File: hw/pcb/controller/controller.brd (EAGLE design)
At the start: 160 x 100 mm, 0 parts

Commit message: Draft of schematic is complete
Still needs review.
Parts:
- added C1, C10, C11, C12, C13, C14, C15, C16, C17, C18, C2, C3, C4, C5, C6, C7, C8, C9: (no value), wedfestdress:CAP_0603
- added D1, D2: (no value), wedfestdress:LED_0603
- added D3: (no value), wedfestdress:LED_0603_OSRAM
- added FB1: (no value), wedfestdress:FB_0603
- added J1: (no value), wedfestdress:10118192-0001LF
- added J10: (no value), wedfestdress:MOLEX_MICROLOCK_RA_2_POS
- added J11: (no value), wedfestdress:MOLEX_MICROLOCK_RA_3_POS
- added J12: (no value), wedfestdress:DF13-3P-1.25H
- added J2: (no value), wedfestdress:MOLEX_MICROFIT_2POS_SMT_RA_W_BOSSES
- added J3: (no value), wedfestdress:DF13-5P-1.25H
- added J4, J5, J6, J7, J8, J9: (no value), wedfestdress:MOLEX_MICROLOCK_RA_4_POS
- added R1, R10, R11, R12, R13, R14, R15, R16, R17, R18, R19, R2, R20, R21, R22, R23, R24, R25, R26, R27, R28, R29, R3, R30, R31, R4, R5, R6, R7, R8, R9: (no value), wedfestdress:RES_0603
- added SW1, SW2, SW3: KMR221NG, wedfestdress:KMR2
- added SW4: CL-SB-22B-12T, wedfestdress:CL-SB-22B-12T
- added TP1, TP10, TP11, TP2, TP3, TP4, TP5, TP6, TP7, TP8, TP9: (no value), wedfestdress:TP_1P6_MM_ROUND
- added TVS1, TVS10, TVS11, TVS12, TVS13, TVS14, TVS15, TVS16, TVS17, TVS18, TVS19, TVS2, TVS20, TVS21, TVS22, TVS23, TVS24, TVS25, TVS26, TVS27, TVS3, TVS4, TVS5, TVS6, TVS7, TVS8, TVS9: (no value), wedfestdress:SOD523
- added U1: (no value), wedfestdress:LQFP64_0P5MM_10X10MM
- added U10, U11, U12, U13, U14, U15, U4, U5, U6, U7, U8, U9: (no value), wedfestdress:SC-70-6_GENERIC
- added U16, U17, U18, U19, U20, U3: (no value), wedfestdress:SOT-23-6_GENERIC
- added U2: (no value), wedfestdress:TOSHIBA_SMV
- added U21: (no value), wedfestdress:SC-70-5_GENERIC
- added U22: (no value), wedfestdress:SOT65P210X110-6N
- added U23: (no value), wedfestdress:ADXL337
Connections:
- new net +6V: C9.P$1, J1.P$1, R1.P$2, TVS26.K
- new net 3V3: C11.P$1, C12.P$1, C13.P$2, C15.P$1, C2.P$1, C3.P$1, C4.P$1, C5.P$1, C6.P$1, C7.P$1, C8.P$1, FB1.P$1, J11.P2, J3.P$1, R17.P$2, R19.P$2, R22.P$2, R23.P$2, R26.P$2, R5.P$2, R6.P$2, R7.P$1, R8.P$2, TP11.P$1, TP5.P$1, TP7.P$1, TVS4.K, U1.24, U1.34, U1.56, U1.8, U10.5, U11.5, U12.5, U13.5, U14.5, U15.5, U2.P5, U21.5, U22.1, U23.P14, U23.P15, U4.5, U5.5, U6.5, U7.5, U8.5, U9.5
- new net ACCEL_TEST: TP1.P$1, U23.P2
- new net ACCEL_XOUT: C18.P$1, U1.14, U23.P5
- new net ACCEL_YOUT: C17.P$1, U1.15, U23.P4
- new net ACCEL_ZOUT: C16.P$1, U1.16, U23.P16
- new net AUX_BTN: R26.P$1, SW3.P1, U1.59
- new net BATT_DIV2: C14.P$1, R24.P$1, R25.P$2, U1.18
- new net CLKOUT: TP6.P$1, U1.61
- new net FC0_MOSI: U1.63, U4.3, U6.3, U8.3
- new net FC0_SCK: U1.60, U5.3, U7.3, U9.3
- new net FC1_RXD: J12.P$2, U1.11
- new net FC1_TXD: J12.P$3, U1.12
- new net FC2_MOSI: U1.43, U10.3, U12.3, U14.3
- new net FC2_SCK: U1.45, U11.3, U13.3, U15.3
- new net FC5_SCL: R23.P$1, U1.54, U22.3
- new net FC5_SDA: R22.P$1, U1.51, U22.4
- new net FC6_RXD: TP3.P$1, U1.39
- new net FC6_TXD: TP2.P$1, U1.40
- new net GND: C1.P$2, C10.P$2, C11.P$2, C12.P$2, C13.P$1, C15.P$2, C16.P$2, C17.P$2, C18.P$2, C2.P$2, C3.P$2, C4.P$2, C5.P$2, C6.P$2, C7.P$2, C8.P$2, C9.P$2, J1.P$5, J10.P1, J11.P1, J12.P$1, J2.P1, J3.P$2, J4.P1, J5.P1, J6.P1, J7.P1, J8.P1, J9.P1, R16.P$1, R18.P$1, R2.P$1, R28.P$1, R29.P$1, R30.P$1, R31.P$1, SW1.P1, SW2.P3, SW3.P3, TP10.P$1, TP4.P$1, TP8.P$1, TP9.P$1, TVS1.A, TVS10.A, TVS11.A, TVS12.A, TVS13.A, TVS14.A, TVS15.A, TVS16.A, TVS17.A, TVS18.A, TVS19.A, TVS2.A, TVS20.A, TVS21.A, TVS22.A, TVS23.A, TVS24.A, TVS25.A, TVS26.A, TVS27.A, TVS3.A, TVS4.A, TVS5.A, TVS6.A, TVS7.A, TVS8.A, TVS9.A, U1.20, U1.21, U1.25, U1.55, U1.9, U10.2, U11.2, U12.2, U13.2, U14.2, U15.2, U16.1, U17.1, U18.1, U19.1, U2.P2, U20.1, U21.2, U22.2, U23.P6, U23.P7, U3.1, U4.2, U5.2, U6.2, U7.2, U8.2, U9.2
- new net GREEN_LED1: D1.A, U1.49
- new net GREEN_LED2: D2.A, U1.50
- new net ISP0: R8.P$1, SW2.P1, U1.13
- new net ISP1: R7.P$2, U1.38
- new net LED_PWR_EN: R16.P$2, U1.36, U20.5, U3.5
- new net MIC_AMP_OUT: R21.P$2, U1.17, U21.4, U22.6
- new net MIC_IN: J11.P3, R20.P$1
- new net N$1: R10.P$2, U3.6
- new net N$10: D3.K, R29.P$2
- new net N$11: D2.K, R30.P$2
- new net N$12: D1.K, R31.P$2
- new net N$16: R15.P$2, U20.6
- new net N$17: R11.P$2, U16.6
- new net N$19: R12.P$2, U17.6
- new net N$2: R3.P$2, U1.5
- new net N$21: R13.P$2, U18.6
- new net N$23: R14.P$2, U19.6
- new net N$3: R4.P$2, U1.6
- new net N$4: J1.P$2, R4.P$1, TVS2.K
- new net N$5: J1.P$3, R3.P$1, R5.P$1, TVS1.K
- new net N$6: R9.P$1, U2.P3
- new net N$7: R20.P$2, R21.P$1, U21.3, U22.5
- new net N$9: C14.P$2, R25.P$1, R27.P$1, R28.P$2
- new net RED_LED1: D3.A, U1.58
- new net RESET_N: J3.P$3, R6.P$1, SW1.P3, TVS5.K, U1.64
- new net STRING1_CLK: J4.P2, TVS23.K, U5.4
- new net STRING1_DATA: J4.P4, TVS25.K, U4.4
- new net STRING1_EN: U1.1, U4.1, U5.1
- new net STRING1_V+: J4.P3, TVS24.K, U3.2, U3.3, U4.6, U5.6
- new net STRING2_CLK: J5.P2, TVS20.K, U7.4
- new net STRING2_DATA: J5.P4, TVS22.K, U6.4
- new net STRING2_EN: U1.2, U6.1, U7.1
- new net STRING2_V+: J5.P3, TVS21.K, U16.2, U16.3, U6.6, U7.6
- new net STRING3_CLK: J6.P2, TVS17.K, U9.4
- new net STRING3_DATA: J6.P4, TVS19.K, U8.4
- new net STRING3_EN: U1.3, U8.1, U9.1
- new net STRING3_V+: J6.P3, TVS18.K, U17.2, U17.3, U8.6, U9.6
- new net STRING4_CLK: J7.P2, TVS14.K, U11.4
- new net STRING4_DATA: J7.P4, TVS16.K, U10.4
- new net STRING4_EN: U1.46, U10.1, U11.1
- new net STRING4_V+: J7.P3, TVS15.K, U10.6, U11.6, U18.2, U18.3
- new net STRING5_CLK: J8.P2, TVS11.K, U13.4
- new net STRING5_DATA: J8.P4, TVS13.K, U12.4
- new net STRING5_EN: U1.47, U12.1, U13.1
- new net STRING5_V+: J8.P3, TVS12.K, U12.6, U13.6, U19.2, U19.3
- new net STRING6_CLK: J9.P2, TVS8.K, U15.4
- new net STRING6_DATA: J9.P4, TVS10.K, U14.4
- new net STRING6_EN: U1.48, U14.1, U15.1
- new net STRING6_V+: J9.P3, TVS9.K, U14.6, U15.6, U20.2, U20.3
- new net SWCLK: J3.P$4, TVS6.K, U1.52
- new net SWDIO: J3.P$5, TVS7.K, U1.53
- new net USB_VBUS: R1.P$1, R2.P$2, U1.26
- new net USER_BTN_IN: J10.P2, R17.P$1, U1.10
- new net VBAT: J2.P2, R10.P$1, R11.P$1, R12.P$1, R13.P$1, R14.P$1, R15.P$1, R24.P$2, SW4.3, SW4.4, TVS27.K, U16.4, U17.4, U18.4, U19.4, U20.4, U3.4
- new net VBAT_READ_EN_R: R27.P$2, U1.42
- new net VBAT_SW: C10.P$1, R9.P$2, SW4.5, SW4.6, TVS3.K, U2.P1
- new net VDDA: C1.P$1, FB1.P$2, U1.22, U1.23
- new net VREF: R18.P$2, R19.P$1, U21.1

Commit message: Routing and silscreen cleanup complete
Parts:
- removed R27, R28: (no value), wedfestdress:RES_0603
- added TP12: (no value), wedfestdress:TP_1P6_MM_ROUND
- added TVS28, TVS29, TVS30: (no value), wedfestdress:SOD523
- moved R31 530.5 mm to (16.8, 38.0)
- moved R30 523.9 mm to (16.8, 35.2)
- moved R29 517.4 mm to (16.8, 32.4)
- moved TP8 517.2 mm to (7.70, 52.3)
- moved D2 514.3 mm to (20.3, 35.2), turned to 180 degrees
- moved TP7 513.2 mm to (29.8, 48.0)
- moved TVS27 513.0 mm to (17.7, 17.7), flipped to the bottom, turned to 135 degrees
- moved R26 509.1 mm to (23.3, 27.1), turned to 270 degrees
- moved TP5 503.6 mm to (52.0, 41.3), turned to 270 degrees
- moved TP10 500.0 mm to (27.5, 27.4)
- moved TP4 498.8 mm to (52.0, 38.9), turned to 270 degrees
- moved TP11 496.2 mm to (36.9, 19.6)
- moved TP6 496.0 mm to (25.8, 33.8)
- moved TP3 493.9 mm to (52.0, 36.5), turned to 270 degrees
- moved TP2 489.0 mm to (52.0, 34.1), turned to 270 degrees
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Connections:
- net N$7 renamed AMP_NEG
- removed net N$9: C14.P$2, R25.P$1, R27.P$1, R28.P$2
- removed net VBAT_READ_EN_R: R27.P$2, U1.42
- net 3V3: now also TP12.P$1, TVS29.K
- net GND: now also C14.P$2, R25.P$1, TVS28.A, TVS29.A, TVS30.A; no longer R28.P$1
- net LED_PWR_EN: now also U16.5, U17.5, U18.5, U19.5
- net MIC_IN: now also TVS30.K
- net STRING1_CLK: now also J4.P3; no longer J4.P2
- net STRING1_V+: now also J4.P2; no longer J4.P3
- net STRING2_CLK: now also J5.P3; no longer J5.P2
- net STRING2_V+: now also J5.P2; no longer J5.P3
- net STRING3_CLK: now also J6.P3; no longer J6.P2
- net STRING3_V+: now also J6.P2; no longer J6.P3
- net STRING4_CLK: now also J7.P3; no longer J7.P2
- net STRING4_V+: now also J7.P2; no longer J7.P3
- net STRING5_CLK: now also J8.P3; no longer J8.P2
- net STRING5_V+: now also J8.P2; no longer J8.P3
- net STRING6_CLK: now also J9.P3; no longer J9.P2
- net STRING6_V+: now also J9.P2; no longer J9.P3
- net USER_BTN_IN: now also TVS28.K
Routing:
- net GND: track 0.00 -> 152.5 mm, vias 0 -> 62
- net 3V3: track 0.00 -> 131.6 mm, vias 0 -> 27
- net LED_PWR_EN: track 0.00 -> 114.0 mm, vias 0 -> 7
- net FC2_MOSI: track 0.00 -> 61.9 mm, vias 0 -> 6
- net FC2_SCK: track 0.00 -> 59.0 mm, vias 0 -> 2
- net STRING6_EN: track 0.00 -> 53.0 mm, vias 0 -> 2
- net N$5: track 0.00 -> 51.9 mm, vias 0 -> 2
- net RESET_N: track 0.00 -> 51.4 mm, vias 0 -> 4
- net FC0_MOSI: track 0.00 -> 50.5 mm, vias 0 -> 6
- net MIC_AMP_OUT: track 0.00 -> 50.0 mm, vias 0 -> 3
- net FC0_SCK: track 0.00 -> 48.7 mm, vias 0 -> 2
- net STRING5_EN: track 0.00 -> 46.4 mm, vias 0 -> 2
- net N$4: track 0.00 -> 46.0 mm, vias 0 -> 2
- net STRING4_EN: track 0.00 -> 43.0 mm, vias 0 -> 2
- net STRING3_EN: track 0.00 -> 35.7 mm, vias 0 -> 2
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- added copper zone on layer 15, net 3V3
- added copper zone on layer 1, net GND
- added copper zone on layer 2, net GND
- added copper zone on layer 1, net VBAT
- added copper zone on layer 15, net VBAT
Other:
- board size 160 x 100 mm -> 60 x 60 mm
- board text added: "+"
- board text added: "+X"
- board text added: "+Y"
- board text added: "+Z"
- board text added: "-"
- board text added: "BAD"
- board text added: "BTN"
- board text added: "BTN2"
- board text added: "ISP"
- board text added: "LED1"
- board text added: "LED2"
- board text added: "MIC"
- board text added: "RESET"
- board text added: "Rev A"
- board text added: "Rx"
- board text added: "S1"
- board text added: "S2"
- board text added: "S3"
- board text added: "S4"
- board text added: "S5"
- board text added: "S6"
- board text added: "Tx"
- board text added: "V+"
- board text added: "Wedfestdress!"

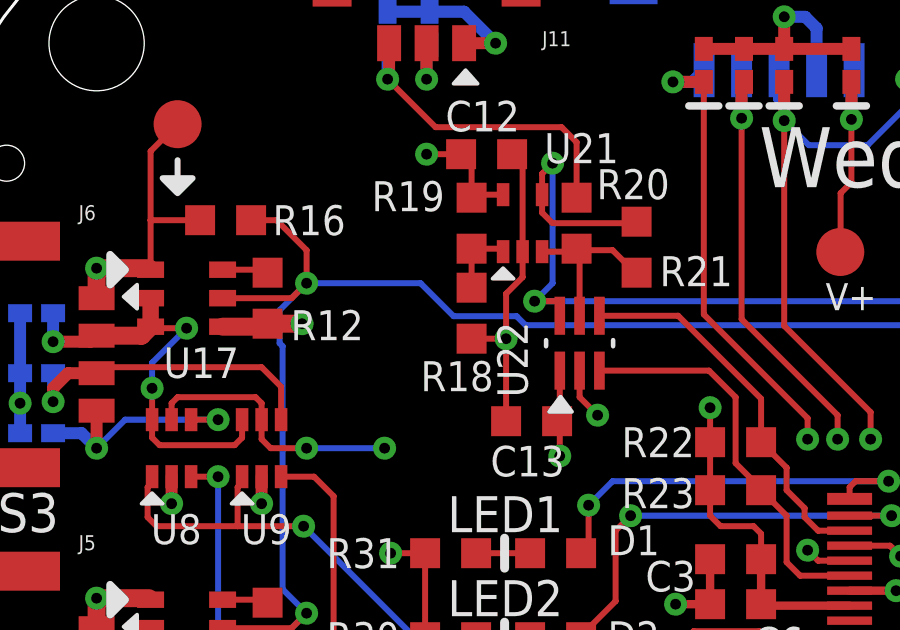
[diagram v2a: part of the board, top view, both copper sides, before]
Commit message: Add microphone board
Completed schematic and layout of microphone board. Is a similar
design to the one from TI's tidu765 app-note. Has provisions for a
more basic non-inverting amplifier design as well. Currently uses a
transimpedence amplifier.
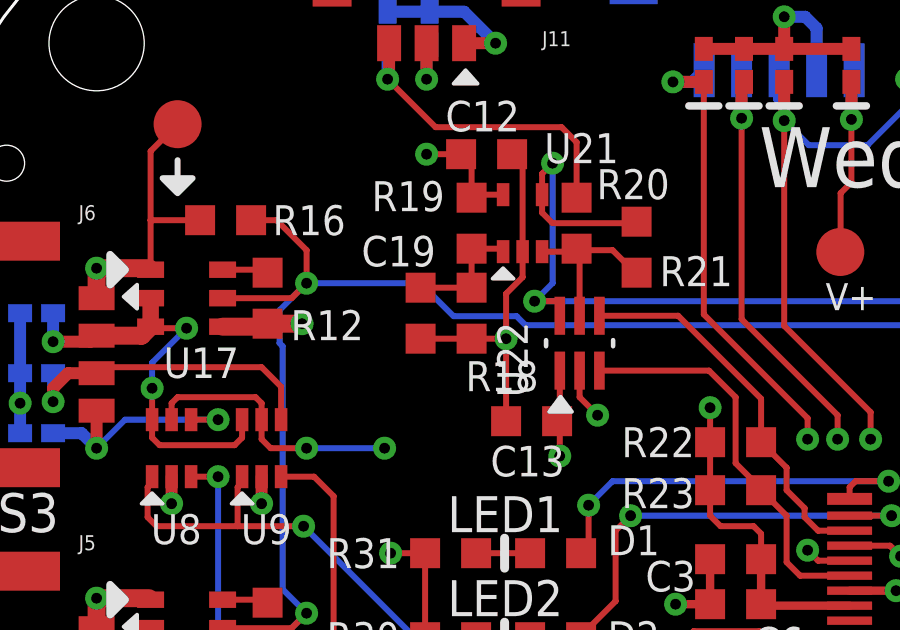
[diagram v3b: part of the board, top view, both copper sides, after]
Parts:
- added C19: (no value), wedfestdress:CAP_0603
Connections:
- net GND: now also C19.P$2
- net VREF: now also C19.P$1
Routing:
- net VREF: track 2.39 -> 4.09 mm
- net GND: track 152.5 -> 154.2 mm
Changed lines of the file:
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@@
 <layer number="21" name="tPlace" color="7" fill="1" visible="yes" active="yes"/>
 <layer number="22" name="bPlace" color="7" fill="1" visible="yes" active="yes"/>
-<layer number="23" name="tOrigins" color="15" fill="1" visible="no" active="yes"/>
+<layer number="23" name="tOrigins" color="15" fill="1" visible="yes" active="yes"/>
 <layer number="24" name="bOrigins" color="15" fill="1" visible="no" active="yes"/>
 <layer number="25" name="tNames" color="7" fill="1" visible="no" active="yes"/>
@@
 <attribute name="NOSTUFF" value="" x="17.5" y="46" size="1.778" layer="27" rot="R90" display="off"/>
 <attribute name="COST_X500" value=".00382" x="17.5" y="46" size="1.778" layer="27" rot="R90" display="off"/>
-<attribute name="NAME" x="18.23" y="44.4" size="1" layer="21" font="vector" rot="R180"/>
+<attribute name="NAME" x="19.73" y="44.4" size="1" layer="21" font="vector" rot="R180"/>
 <attribute name="NAME" x="18.5" y="47.27" size="1" layer="105" font="vector" rot="R90"/>
 </element>
@@
 <attribute name="COST_X500" value="0.22626" x="14.7" y="55.5" size="1.778" layer="28" rot="MR270" display="off"/>
 </element>
+<element name="C19" library="wedfestdress" package="CAP_0603" value="" x="15.8" y="46" smashed="yes" rot="R270">
+<attribute name="PACKAGE" value="0603" x="15.8" y="46" size="0.9" layer="27" font="vector" ratio="10" rot="R270" display="off"/>
+<attribute name="DIST_PART_NO" value="490-3894-1-ND" x="15.8" y="46" size="0.9" layer="27" font="vector" ratio="10" rot="R270" display="off"/>
+<attribute name="COST_X1" value="0.11" x="15.8" y="46" size="0.9" layer="27" font="vector" ratio="10" rot="R270" display="off"/>
+<attribute name="DISTRIBUTOR" value="Digikey" x="15.8" y="46" size="0.9" layer="27" font="vector" ratio="10" rot="R270" display="off"/>
+<attribute name="DESCRIPTION" value="Capacitor, 1 uF, 16V, 0603, X5R" x="15.8" y="46" size="0.9" layer="27" font="vector" ratio="10" rot="R270" display="off"/>
+<attribute name="DISPLAY" value="1 uF, 50V" x="15.8" y="46" size="0.9" layer="27" font="vector" ratio="10" rot="R270" display="off"/>
+<attribute name="COST_X100" value="0.0356" x="15.8" y="46" size="0.9" layer="27" font="vector" ratio="10" rot="R270" display="off"/>
+<attribute name="MFG" value="Murata" x="15.8" y="46" size="0.9" layer="27" font="vector" ratio="10" rot="R270" display="off"/>
+<attribute name="MFG_PART_NO" value="GRM185R61C105KE44D" x="15.8" y="46" size="0.9" layer="27" font="vector" ratio="10" rot="R270" display="off"/>
+<attribute name="NOSTUFF" value="" x="15.8" y="46" size="0.9" layer="27" font="vector" ratio="10" rot="R270" display="off"/>
+<attribute name="COST_X500" value="0.02512" x="15.8" y="46" size="0.9" layer="27" font="vector" ratio="10" rot="R270" display="off"/>
+<attribute name="NAME" x="13.83" y="47.56" size="1.016" layer="21" font="vector"/>
+</element>
 </elements>
 <signals>
@@
 <wire x1="27.49" y1="27.42" x2="28.8" y2="28.73" width="0.2" layer="1"/>
 <via x="28.8" y="28.73" extent="1-16" drill="0.36" diameter="0.61"/>
+<contactref element="C19" pad="P$2"/>
+<wire x1="15.8" y1="45.15" x2="17.5" y2="45.15" width="0.2" layer="1"/>
 </signal>
 <signal name="3V3">
@@
 <wire x1="17.5" y1="48.15" x2="18.45" y2="48.15" width="0.2" layer="1"/>
 <wire x1="18.45" y1="48.15" x2="18.55" y2="48.05" width="0.2" layer="1"/>
+<contactref element="C19" pad="P$1"/>
+<wire x1="15.8" y1="46.85" x2="17.5" y2="46.85" width="0.2" layer="1"/>
 </signal>
 <signal name="MIC_AMP_OUT">

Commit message: Final tweaks and CAM output for all three boards
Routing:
- net GND: track 154.2 -> 153.0 mm, vias 62 -> 63
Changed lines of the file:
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@@
 <layer number="29" name="tStop" color="7" fill="3" visible="yes" active="yes"/>
 <layer number="30" name="bStop" color="7" fill="6" visible="yes" active="yes"/>
-<layer number="31" name="tCream" color="7" fill="4" visible="no" active="yes"/>
-<layer number="32" name="bCream" color="7" fill="5" visible="no" active="yes"/>
+<layer number="31" name="tCream" color="7" fill="4" visible="yes" active="yes"/>
+<layer number="32" name="bCream" color="7" fill="5" visible="yes" active="yes"/>
 <layer number="33" name="tFinish" color="6" fill="3" visible="no" active="yes"/>
 <layer number="34" name="bFinish" color="6" fill="6" visible="no" active="yes"/>
@@
 <wire x1="44.25" y1="54.1" x2="44.25" y2="53.05" width="0.2" layer="16"/>
 <wire x1="44.25" y1="53.05" x2="44.8" y2="52.5" width="0.2" layer="16"/>
-<wire x1="52.3" y1="7.7" x2="52.1" y2="7.5" width="0.2" layer="1"/>
-<wire x1="52.1" y1="7.5" x2="49.5" y2="7.5" width="0.2" layer="1"/>
 <wire x1="7.7" y1="52.3" x2="6.8" y2="51.4" width="0.2" layer="1"/>
 <wire x1="6.8" y1="51.4" x2="6.8" y2="49.1" width="0.2" layer="1"/>
@@
 <contactref element="C19" pad="P$2"/>
 <wire x1="15.8" y1="45.15" x2="17.5" y2="45.15" width="0.2" layer="1"/>
+<wire x1="52.3" y1="7.7" x2="52.3" y2="9.3" width="0.2" layer="1"/>
+<via x="52.3" y="9.3" extent="1-16" drill="0.36" diameter="0.61"/>
 </signal>
 <signal name="3V3">
